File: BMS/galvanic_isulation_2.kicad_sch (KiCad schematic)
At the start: 12 parts

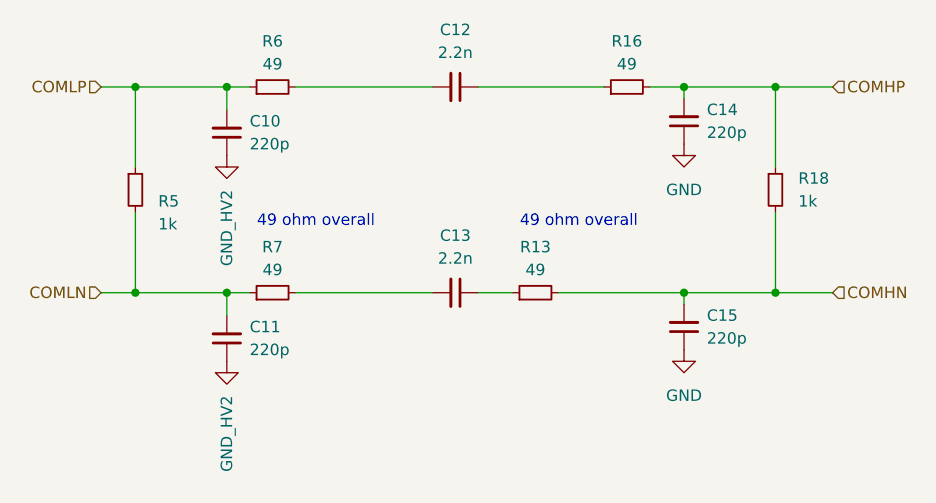
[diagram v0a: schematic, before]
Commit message: Dodano layout drugiego bq79614, ukladu tlumaczącego z protokułu TI na UART oraz wstępnie poprowadzono pary różnicowe
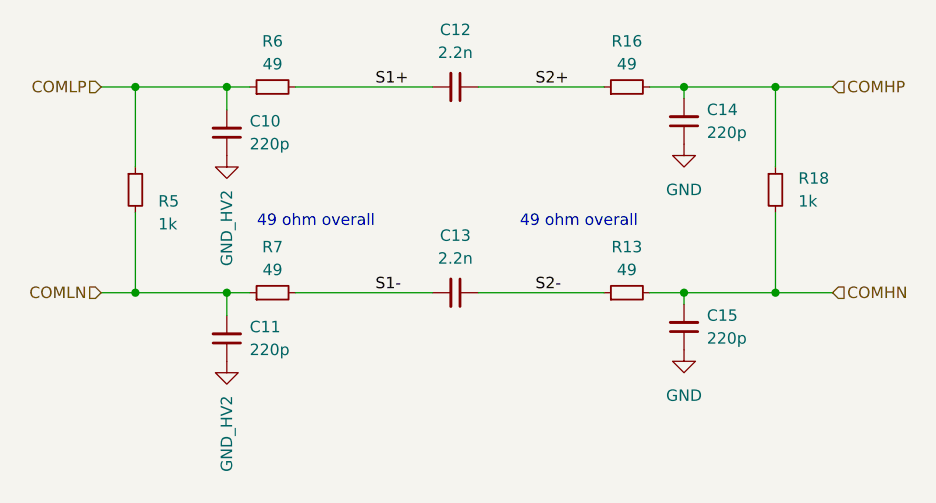
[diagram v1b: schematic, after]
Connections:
- net S2+: now reaches C12.1, R16.1
- net S2-: now reaches C13.1, R13.1
- net S1+: now reaches C12.2, R6.2
- net S1-: now reaches C13.2, R7.2
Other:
- moved on the sheet: R13
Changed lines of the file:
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@@
-	(wire
-		(pts
-			(xy 130.81 105.41) (xy 127 105.41)
-		)
-		(stroke
-			(width 0)
-			(type default)
-		)
-	)
 	(wire
 		(pts
@@
 	(wire
 		(pts
+			(xy 127 105.41) (xy 140.97 105.41)
+		)
+		(stroke
+			(width 0)
+			(type default)
+		)
+	)
+	(wire
+		(pts
 			(xy 99.06 105.41) (xy 99.06 107.95)
 		)
@@
 	(wire
 		(pts
-			(xy 135.89 105.41) (xy 149.86 105.41)
+			(xy 146.05 105.41) (xy 149.86 105.41)
 		)
 		(stroke
@@
 				(size 1.27 1.27)
 			)
+		)
+	)
+	(label "S2-"
+		(at 133.35 105.41 0)
+		(fields_autoplaced yes)
+		(effects
+			(font
+				(size 1.27 1.27)
+			)
+			(justify left bottom)
+		)
+	)
+	(label "S1+"
+		(at 115.57 82.55 0)
+		(fields_autoplaced yes)
+		(effects
+			(font
+				(size 1.27 1.27)
+			)
+			(justify left bottom)
+		)
+	)
+	(label "S2+"
+		(at 133.35 82.55 0)
+		(fields_autoplaced yes)
+		(effects
+			(font
+				(size 1.27 1.27)
+			)
+			(justify left bottom)
+		)
+	)
+	(label "S1-"
+		(at 115.57 105.41 0)
+		(fields_autoplaced yes)
+		(effects
+			(font
+				(size 1.27 1.27)
+			)
+			(justify left bottom)
 		)
 	)
@@
 	(symbol
 		(lib_id "Device:R_Small")
-		(at 133.35 105.41 90)
+		(at 143.51 105.41 90)
 		(unit 1)
 		(exclude_from_sim no)
@@
 		(fields_autoplaced yes)
 		(property "Reference" "R13"
-			(at 133.35 100.33 90)
+			(at 143.51 100.33 90)
 			(effects
 				(font
@@
 		)
 		(property "Value" "49"
-			(at 133.35 102.87 90)
+			(at 143.51 102.87 90)
 			(effects
 				(font
@@
 		)
 		(property "Footprint" "Resistor_SMD:R_0603_1608Metric_Pad0.98x0.95mm_HandSolder"
-			(at 133.35 105.41 0)
+			(at 143.51 105.41 0)
 			(effects
 				(font
@@
 		)
 		(property "Datasheet" "https://www.mouser.pl/ProductDetail/KOA-Speer/RK73H1HRTTCM49R9F?qs=sGAEpiMZZMvdGkrng054txLI%2FDB4oIKDjd1z9Y%252BmyaXFChdzxTCbsQ%3D%3D"
-			(at 133.35 105.41 0)
+			(at 143.51 105.41 0)
 			(effects
 				(font
@@
 		)
 		(property "Description" "Resistor, small symbol"
-			(at 133.35 105.41 0)
-			(effects
-				(font
+			(at 143.51 105.41 0)
+			(effects
+				(font

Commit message: poprawy
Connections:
- net GND: now also C10.1, C11.1; no longer C14.1, C15.1
- net GND_HV2: now also C14.1, C15.1; no longer C10.1, C11.1
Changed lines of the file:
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@@
 	(symbol
 		(lib_id "power:GND")
-		(at 149.86 88.9 0)
+		(at 99.06 90.17 0)
 		(unit 1)
 		(exclude_from_sim no)
@@
 		(fields_autoplaced yes)
 		(property "Reference" "#PWR025"
-			(at 149.86 95.25 0)
+			(at 99.06 96.52 0)
 			(effects
 				(font
@@
 		)
 		(property "Value" "GND"
-			(at 149.86 93.98 0)
+			(at 99.06 95.25 0)
 			(effects
 				(font
@@
 		)
 		(property "Footprint" ""
-			(at 149.86 88.9 0)
+			(at 99.06 90.17 0)
 			(effects
 				(font
@@
 		)
 		(property "Datasheet" ""
-			(at 149.86 88.9 0)
+			(at 99.06 90.17 0)
 			(effects
 				(font
@@
 		)
 		(property "Description" "Power symbol creates a global label with name \"GND\" , ground"
-			(at 149.86 88.9 0)
+			(at 99.06 90.17 0)
 			(effects
 				(font
@@
 	(symbol
 		(lib_id "power:GND")
-		(at 99.06 90.17 0)
+		(at 149.86 88.9 0)
 		(unit 1)
 		(exclude_from_sim no)
@@
 		(dnp no)
 		(property "Reference" "#PWR023"
-			(at 99.06 96.52 0)
+			(at 149.86 95.25 0)
 			(effects
 				(font
@@
 		)
 		(property "Value" "GND_HV2"
-			(at 99.06 93.98 90)
+			(at 149.86 92.71 90)
 			(effects
 				(font
@@
 		)
 		(property "Footprint" ""
-			(at 99.06 90.17 0)
+			(at 149.86 88.9 0)
 			(effects
 				(font
@@
 		)
 		(property "Datasheet" ""
-			(at 99.06 90.17 0)
+			(at 149.86 88.9 0)
 			(effects
 				(font
@@
 		)
 		(property "Description" "Power symbol creates a global label with name \"GND\" , ground"
-			(at 99.06 90.17 0)
+			(at 149.86 88.9 0)
 			(effects
 				(font
@@
 	(symbol
 		(lib_id "power:GND")
+		(at 149.86 111.76 0)
+		(unit 1)
+		(exclude_from_sim no)
+		(in_bom yes)
+		(on_board yes)
+		(dnp no)
+		(property "Reference" "#PWR024"
+			(at 149.86 118.11 0)
+			(effects
+				(font
+					(size 1.27 1.27)
+				)
+				(hide yes)
+			)
+		)
+		(property "Value" "GND_HV2"
+			(at 149.86 115.57 90)
+			(effects
+				(font
+					(size 1.27 1.27)
+				)
+				(justify right)
+			)
+		)
+		(property "Footprint" ""
+			(at 149.86 111.76 0)
+			(effects
+				(font
+					(size 1.27 1.27)
+				)
+				(hide yes)
+			)
+		)
+		(property "Datasheet" ""
+			(at 149.86 111.76 0)
+			(effects
+				(font
+					(size 1.27 1.27)
+				)
+				(hide yes)
+			)
+		)
+		(property "Description" "Power symbol creates a global label with name \"GND\" , ground"
+			(at 149.86 111.76 0)
+			(effects
+				(font
+					(size 1.27 1.27)
+				)
+				(hide yes)
+			)
+		)
+		(pin "1"
+		)
+		(instances
+			(project "BMS"
+				(path "/26289bb6-56bc-4ca1-b1a2-18d58d1afdf5/1b8fbd81-7ef0-462a-a785-6c377cb64ff7"
+					(reference "#PWR024")
+					(unit 1)
+				)
+			)
+		)
+	)
+	(symbol
+		(lib_id "power:GND")
 		(at 99.06 113.03 0)
 		(unit 1)
@@
 		(on_board yes)
 		(dnp no)
-		(property "Reference" "#PWR024"
+		(fields_autoplaced yes)
+		(property "Reference" "#PWR026"
 			(at 99.06 119.38 0)
 			(effects
@@
 			)
 		)
-		(property "Value" "GND_HV2"
-			(at 99.06 116.84 90)
-			(effects
-				(font
-					(size 1.27 1.27)
-				)
-				(justify right)
+		(property "Value" "GND"
+			(at 99.06 118.11 0)
+			(effects
+				(font
+					(size 1.27 1.27)
+				)
 			)
 		)
@@
 			(effects
 				(font
-					(size 1.27 1.27)
-				)
-				(hide yes)
-			)
-		)
-		(pin "1"
-		)
-		(instances
-			(project "BMS"
-				(path "/26289bb6-56bc-4ca1-b1a2-18d58d1afdf5/1b8fbd81-7ef0-462a-a785-6c377cb64ff7"
-					(reference "#PWR024")
-					(unit 1)
-				)
-			)
-		)
-	)
-	(symbol
-		(lib_id "power:GND")
-		(at 149.86 111.76 0)
-		(unit 1)
-		(exclude_from_sim no)
-		(in_bom yes)
-		(on_board yes)
-		(dnp no)
-		(fields_autoplaced yes)
-		(property "Reference" "#PWR026"
-			(at 149.86 118.11 0)
-			(effects
-				(font
-					(size 1.27 1.27)
-				)
-				(hide yes)
-			)
-		)
-		(property "Value" "GND"
-			(at 149.86 116.84 0)
-			(effects
-				(font
-					(size 1.27 1.27)
-				)
-			)
-		)
-		(property "Footprint" ""
-			(at 149.86 111.76 0)
-			(effects
-				(font
-					(size 1.27 1.27)
-				)
-				(hide yes)
-			)
-		)
-		(property "Datasheet" ""
-			(at 149.86 111.76 0)
-			(effects
-				(font
-					(size 1.27 1.27)
-				)
-				(hide yes)
-			)
-		)
-		(property "Description" "Power symbol creates a global label with name \"GND\" , ground"
-			(at 149.86 111.76 0)
-			(effects
-				(font

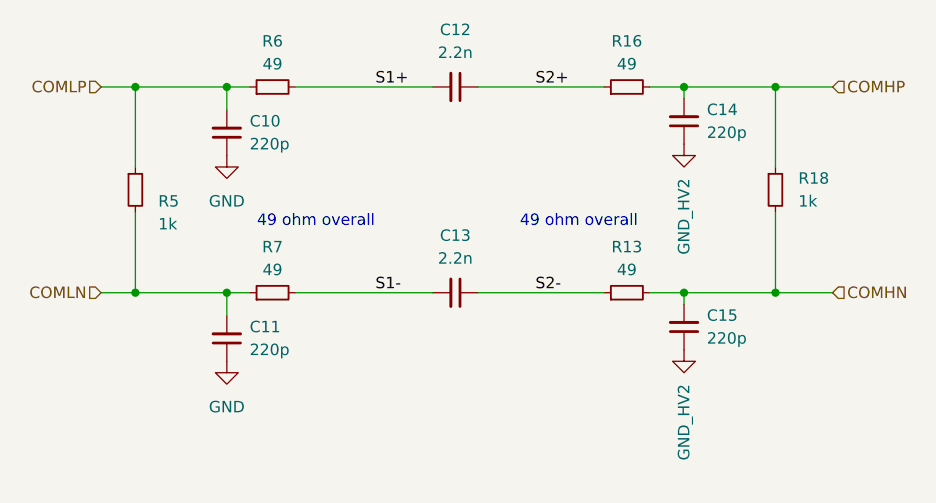
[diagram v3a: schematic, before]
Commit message: Zmienione kondensatory na kondensatory bezpieczeństwa,poprawiono strefy na thermal relief oraz naprawiono bledy z tym zwiazane, impedancja do zmiany jeszcze
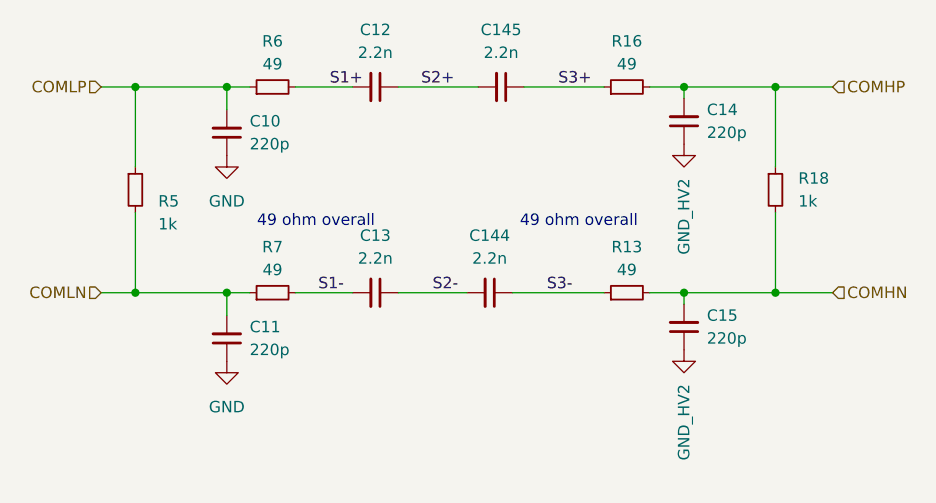
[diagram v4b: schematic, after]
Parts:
- added C144, C145: 2.2n, footrpint:CAPC5728X280N, symbol Device:C_Small
- C12, C13: footprint Capacitor_SMD:C_0603_1608Metric_Pad1.08x0.95mm_HandSolder -> footrpint:CAPC5728X280N
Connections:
- net S2+: now also C145.2; no longer R16.1
- net S2-: now also C144.2; no longer R13.1
- new net S3+: C145.1, R16.1
- new net S3-: C144.1, R13.1
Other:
- moved on the sheet: C12, C13
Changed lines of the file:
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@@
+	(wire
+		(pts
+			(xy 130.81 105.41) (xy 140.97 105.41)
+		)
+		(stroke
+			(width 0)
+			(type default)
+		)
+	)
 	(wire
 		(pts
@@
 	(wire
 		(pts
-			(xy 106.68 105.41) (xy 121.92 105.41)
+			(xy 106.68 105.41) (xy 113.03 105.41)
 		)
 		(stroke
@@
 	(wire
 		(pts
+			(xy 118.11 82.55) (xy 127 82.55)
+		)
+		(stroke
+			(width 0)
+			(type default)
+		)
+	)
+	(wire
+		(pts
 			(xy 88.9 82.55) (xy 88.9 91.44)
 		)
@@
 	(wire
 		(pts
+			(xy 132.08 82.55) (xy 140.97 82.55)
+		)
+		(stroke
+			(width 0)
+			(type default)
+		)
+	)
+	(wire
+		(pts
 			(xy 149.86 106.68) (xy 149.86 105.41)
 		)
@@
 	(wire
 		(pts
-			(xy 106.68 82.55) (xy 121.92 82.55)
+			(xy 106.68 82.55) (xy 113.03 82.55)
 		)
 		(stroke
@@
 	(wire
 		(pts
-			(xy 127 105.41) (xy 140.97 105.41)
-		)
-		(stroke
-			(width 0)
-			(type default)
-		)
-	)
-	(wire
-		(pts
 			(xy 99.06 105.41) (xy 99.06 107.95)
 		)
@@
 	(wire
 		(pts
-			(xy 127 82.55) (xy 140.97 82.55)
+			(xy 118.11 105.41) (xy 125.73 105.41)
 		)
 		(stroke
@@
 	)
 	(label "S2-"
-		(at 133.35 105.41 0)
+		(at 121.92 105.41 0)
 		(effects
 			(font
@@
 		)
 	)
-	(label "S1+"
-		(at 115.57 82.55 0)
+	(label "S2+"
+		(at 120.65 82.55 0)
 		(effects
 			(font
@@
 		)
 	)
-	(label "S2+"
-		(at 133.35 82.55 0)
+	(label "S3-"
+		(at 134.62 105.41 0)
 		(effects
 			(font
@@
 		)
 	)
+	(label "S1+"
+		(at 110.49 82.55 0)
+		(effects
+			(font
+				(size 1.27 1.27)
+			)
+			(justify left bottom)
+		)
+	)
+	(label "S3+"
+		(at 135.89 82.55 0)
+		(effects
+			(font
+				(size 1.27 1.27)
+			)
+			(justify left bottom)
+		)
+	)
 	(label "S1-"
-		(at 115.57 105.41 0)
+		(at 109.22 105.41 0)
 		(effects
 			(font
@@
 	(symbol
 		(lib_id "Device:C_Small")
-		(at 124.46 82.55 270)
+		(at 115.57 82.55 270)
 		(unit 1)
 		(exclude_from_sim no)
@@
 		(fields_autoplaced yes)
 		(property "Reference" "C12"
-			(at 124.4536 76.2 90)
+			(at 115.5636 76.2 90)
 			(effects
 				(font
@@
 		)
 		(property "Value" "2.2n"
-			(at 124.4536 78.74 90)
-			(effects
-				(font
-					(size 1.27 1.27)
-				)
-			)
-		)
-		(property "Footprint" "Capacitor_SMD:C_0603_1608Metric_Pad1.08x0.95mm_HandSolder"
-			(at 124.46 82.55 0)
-			(effects
-				(font
-					(size 1.27 1.27)
-				)
-				(hide yes)
-			)
-		)
-		(property "Datasheet" "https://www.mouser.pl/ProductDetail/TDK/CGA3E2C0G1H222J080AE?qs=P1JMDcb91o5KNu2GzASXrQ%3D%3D"
-			(at 124.46 82.55 0)
-			(effects
-				(font
-					(size 1.27 1.27)
-				)
-				(hide yes)
-			)
-		)
-		(property "Description" "Unpolarized capacitor, small symbol"
-			(at 124.46 82.55 0)
+			(at 115.5636 78.74 90)
+			(effects
+				(font
+					(size 1.27 1.27)
+				)
+			)
+		)
+		(property "Footprint" "footrpint:CAPC5728X280N"
+			(at 115.57 82.55 0)
+			(effects
+				(font
+					(size 1.27 1.27)
+				)
+				(hide yes)
+			)
+		)
+		(property "Datasheet" "https://www.mouser.pl/ProductDetail/Walsin/S252B222K502CT?qs=wUXugUrL1qx2Bha0j7hz5g%3D%3D"
+			(at 115.57 82.55 0)
+			(effects
+				(font
+					(size 1.27 1.27)
+				)
+				(hide yes)
+			)
+		)
+		(property "Description" "Kondensator Bezpieczeństwa 250V"
+			(at 115.57 82.55 0)
 			(effects
 				(font
@@
 				(path "/26289bb6-56bc-4ca1-b1a2-18d58d1afdf5/1b8fbd81-7ef0-462a-a785-6c377cb64ff7"
 					(reference "C12")
+					(unit 1)
+				)
+			)
+		)
+	)
+	(symbol
+		(lib_id "Device:C_Small")
+		(at 129.54 82.55 270)
+		(unit 1)
+		(exclude_from_sim no)
+		(in_bom yes)
+		(on_board yes)
+		(dnp no)
+		(fields_autoplaced yes)
+		(property "Reference" "C145"
+			(at 129.5336 76.2 90)
+			(effects
+				(font
+					(size 1.27 1.27)
+				)
+			)
+		)
+		(property "Value" "2.2n"
+			(at 129.5336 78.74 90)
+			(effects
+				(font
+					(size 1.27 1.27)
+				)
+			)
+		)
+		(property "Footprint" "footrpint:CAPC5728X280N"
+			(at 129.54 82.55 0)
+			(effects
+				(font
+					(size 1.27 1.27)
+				)
+				(hide yes)
+			)
+		)
+		(property "Datasheet" "https://www.mouser.pl/ProductDetail/Walsin/S252B222K502CT?qs=wUXugUrL1qx2Bha0j7hz5g%3D%3D"
+			(at 129.54 82.55 0)
+			(effects
+				(font
+					(size 1.27 1.27)
+				)
+				(hide yes)
+			)
+		)
+		(property "Description" "Kondensator Bezpieczeństwa 250V"
+			(at 129.54 82.55 0)
+			(effects
+				(font
+					(size 1.27 1.27)
+				)
+				(hide yes)
+			)
+		)
+		(pin "2"
+		)
+		(pin "1"
+		)
+		(instances
+			(project "BMS"
+				(path "/26289bb6-56bc-4ca1-b1a2-18d58d1afdf5/1b8fbd81-7ef0-462a-a785-6c377cb64ff7"
+					(reference "C145")
 					(unit 1)
 				)
@@
 	(symbol
 		(lib_id "Device:C_Small")
+		(at 128.27 105.41 270)
+		(unit 1)
+		(exclude_from_sim no)
+		(in_bom yes)
+		(on_board yes)
+		(dnp no)
+		(fields_autoplaced yes)
+		(property "Reference" "C144"
+			(at 128.2636 99.06 90)
+			(effects
+				(font
+					(size 1.27 1.27)
+				)
+			)
+		)
+		(property "Value" "2.2n"
+			(at 128.2636 101.6 90)
+			(effects
+				(font
+					(size 1.27 1.27)
+				)
+			)
+		)
+		(property "Footprint" "footrpint:CAPC5728X280N"
+			(at 128.27 105.41 0)
+			(effects
+				(font
+					(size 1.27 1.27)
+				)
+				(hide yes)
+			)
+		)
+		(property "Datasheet" "https://www.mouser.pl/ProductDetail/Walsin/S252B222K502CT?qs=wUXugUrL1qx2Bha0j7hz5g%3D%3D"
+			(at 128.27 105.41 0)
+			(effects
+				(font
+					(size 1.27 1.27)
+				)
+				(hide yes)
+			)
+		)
+		(property "Description" "Kondensator Bezpieczeństwa 250V"
+			(at 128.27 105.41 0)
+			(effects
+				(font
+					(size 1.27 1.27)
+				)
+				(hide yes)
+			)
+		)
+		(pin "2"
+		)
+		(pin "1"
+		)
+		(instances
+			(project "BMS"
+				(path "/26289bb6-56bc-4ca1-b1a2-18d58d1afdf5/1b8fbd81-7ef0-462a-a785-6c377cb64ff7"
+					(reference "C144")
+					(unit 1)
+				)
+			)
+		)
+	)
+	(symbol
+		(lib_id "Device:C_Small")
 		(at 149.86 109.22 180)
 		(unit 1)
@@
 	(symbol
 		(lib_id "Device:C_Small")
-		(at 124.46 105.41 270)
+		(at 115.57 105.41 270)
 		(unit 1)
 		(exclude_from_sim no)
@@
 		(fields_autoplaced yes)
 		(property "Reference" "C13"
-			(at 124.4536 99.06 90)
+			(at 115.5636 99.06 90)
 			(effects
 				(font
@@
 		)
 		(property "Value" "2.2n"
-			(at 124.4536 101.6 90)
-			(effects
-				(font
-					(size 1.27 1.27)
-				)
-			)
-		)
-		(property "Footprint" "Capacitor_SMD:C_0603_1608Metric_Pad1.08x0.95mm_HandSolder"
-			(at 124.46 105.41 0)
-			(effects
-				(font
-					(size 1.27 1.27)
-				)
-				(hide yes)
-			)
-		)
-		(property "Datasheet" "https://www.mouser.pl/ProductDetail/TDK/CGA3E2C0G1H222J080AE?qs=P1JMDcb91o5KNu2GzASXrQ%3D%3D"
-			(at 124.46 105.41 0)
-			(effects
-				(font
-					(size 1.27 1.27)
-				)
-				(hide yes)
-			)
-		)
-		(property "Description" "Unpolarized capacitor, small symbol"
-			(at 124.46 105.41 0)
-			(effects
-				(font
+			(at 115.5636 101.6 90)
+			(effects
+				(font
+					(size 1.27 1.27)
+				)
+			)
+		)
+		(property "Footprint" "footrpint:CAPC5728X280N"
+			(at 115.57 105.41 0)
+			(effects
+				(font
+					(size 1.27 1.27)
+				)
+				(hide yes)
+			)
+		)
+		(property "Datasheet" "https://www.mouser.pl/ProductDetail/Walsin/S252B222K502CT?qs=wUXugUrL1qx2Bha0j7hz5g%3D%3D"
+			(at 115.57 105.41 0)
+			(effects
+				(font
+					(size 1.27 1.27)
+				)
+				(hide yes)
+			)
+		)
+		(property "Description" "Kondensator Bezpieczeństwa 250V"
+			(at 115.57 105.41 0)
+			(effects
+				(font
